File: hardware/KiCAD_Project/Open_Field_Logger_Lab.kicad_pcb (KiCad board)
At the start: 2 copper layers, 0 parts

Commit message: Initial PCB Layout
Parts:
- added BT1: 1-0000863, batteries:1-0000863, F.Cu at (133.6, 86.0)
- added C1: 1-0000007, capacitors_0603:1-0000007, F.Cu at (132.9, 113.2)
- added C16: 1-0000007, capacitors_0603:1-0000007, F.Cu at (171.7, 113.8)
- added C2: 1-0000007, capacitors_0603:1-0000007, F.Cu at (149.6, 105.3)
- added C3: 1-0001902, capacitors_0603:1-0001902, F.Cu at (137.2, 107.7)
- added C4: 1-0001902, capacitors_0603:1-0001902, F.Cu at (137.2, 110.5)
- added C5: 1-0000019, capacitors_0603:1-0000019, F.Cu at (102.6, 87.2)
- added D1: 1-0000600, leds_0805:1-0000600, F.Cu at (168.9, 69.1)
- added D2: 1-0000599, leds_0805:1-0000599, F.Cu at (179.1, 69.1)
- added D3: 1-0001188, leds_th:1-0001188, F.Cu at (191.8, 69.1)
- added D4: 1-0001896, diodes:1-0001896, F.Cu at (116.2, 97.7)
- added FID1: Fiducial_1mm_2mm, mechanical:Fiducial_1mm_Mask2mm, F.Cu at (101.0, 129.5)
- added FID2: Fiducial_1mm_2mm, mechanical:Fiducial_1mm_Mask2mm, F.Cu at (198.1, 70.6)
- added G***: LOGO, pcb_graphics:PCB Logo Standard, F.Cu at (104.6, 69.5)
- added H1: Imperial4, mechanical:MountingHole_imperial4, F.Cu at (96.5, 129.5)
- added H2: Imperial4, mechanical:MountingHole_imperial4, F.Cu at (198.1, 66.0)
- added H3: Imperial4, mechanical:MountingHole_imperial4, F.Cu at (96.5, 66.0)
- added H4: Imperial4, mechanical:MountingHole_imperial4, F.Cu at (198.1, 129.5)
- added J1: 1-0001899, connectors:1-0001899, F.Cu at (97.3, 97.8)
- added J10: 1-0001894, connectors:1-0001894, F.Cu at (109.3, 93.2)
- added J11: 1-0000127, connectors:1-0000127, F.Cu at (161.4, 116.0)
- added J12: NP_Conn_01x06, np_connectors:PinHeader_1x06_P2.54mm_Vertical, F.Cu at (177.5, 130.6)
- added J13: NP_Conn_01x03, np_connectors:PinHeader_1x03_P2.54mm_Vertical, F.Cu at (148.0, 64.9)
- added J14: AUX Input, np_connectors:PinHeader_1x04_P2.54mm_Vertical, F.Cu at (157.0, 105.8)
- added J2: 1-0001899, connectors:1-0001899, F.Cu at (109.5, 128.8)
- added J3: 1-0001899, connectors:1-0001899, F.Cu at (119.9, 128.8)
- added J4: 1-0001899, connectors:1-0001899, F.Cu at (130.3, 128.8)
- added J5: 1-0001899, connectors:1-0001899, F.Cu at (140.7, 128.8)
- added J6: 1-0001899, connectors:1-0001899, F.Cu at (151.1, 128.8)
- added J7: Conn_01x01, np_connectors:NP_Conn_ProtoPad, F.Cu at (96.5, 118.4)
- added J8: NP_Conn_01x04, np_connectors:PinHeader_1x04_P2.54mm_Vertical, F.Cu at (199.1, 122.2)
- added J9: 1-0001894, connectors:1-0001894, F.Cu at (109.3, 102.3)
- added MI1: 1-0001895, misc:misc_component, F.Cu at (109.3, 97.5)
- added PCB1: barepcb, misc:barepcb, F.Cu at (162.9, 169.9)
- added Q1: 1-0000163, mosfets:1-0000163, F.Cu at (127.5, 107.7)
- added Q2: 1-0000163, mosfets:1-0000163, F.Cu at (132.1, 107.7)
- added Q3: 1-0000163, mosfets:1-0000163, F.Cu at (122.9, 107.7)
- added R1: 1-0001184, resistors_0603:1-0001184, F.Cu at (107.2, 114.6)
- added R10: 1-0000010, resistors_0603:1-0000010, F.Cu at (127.5, 110.2)
- added R11: 1-0000010, resistors_0603:1-0000010, F.Cu at (122.9, 105.2)
- added R12: 1-0000010, resistors_0603:1-0000010, F.Cu at (122.9, 110.2)
- added R13: 1-0000174, resistors_0603:1-0000174, F.Cu at (171.7, 112.0)
- added R14: 1-0000010, resistors_0603:1-0000010, F.Cu at (159.0, 127.3)
- added R15: 1-0000010, resistors_0603:1-0000010, F.Cu at (152.6, 108.8)
- added R2: 1-0000008, resistors_0603:1-0000008, F.Cu at (165.6, 69.1)
- added R20: 1-0000174, resistors_0603:1-0000174, F.Cu at (161.8, 113.8)
- added R21: 1-0000010, resistors_0603:1-0000010, F.Cu at (132.1, 105.2)
- added R24: 1-0000010, resistors_0603:1-0000010, F.Cu at (132.1, 110.2)
- added R3: 1-0000008, resistors_0603:1-0000008, F.Cu at (175.8, 69.1)
- added R4: 1-0000369, resistors_0603:1-0000369, F.Cu at (185.7, 69.1)
- added R5: 1-0000010, resistors_0603:1-0000010, F.Cu at (131.3, 116.5)
- added R6: 1-0000010, resistors_0603:1-0000010, F.Cu at (129.8, 116.5)
- added R7: 1-0000010, resistors_0603:1-0000010, F.Cu at (125.2, 116.5)
- added R8: 1-0000010, resistors_0603:1-0000010, F.Cu at (123.7, 116.5)
- added R9: 1-0000010, resistors_0603:1-0000010, F.Cu at (127.5, 105.2)
- added SW1: 1-0000681, switches:1-0000681, F.Cu at (156.2, 69.1)
- added TH1: 1-0001897, sensors:1-0001897, F.Cu at (95.5, 114.6)
- added U1: 1-0001891, adcs:1-0001891, F.Cu at (127.5, 113.2)
- added U2: 1-0001892, rtcs:1-0001892, F.Cu at (142.7, 107.9)
- added U3: 1-0001893, dc_dc_converters:1-0001893, F.Cu at (106.9, 83.7)
- added U4: 1-0001890, microcontrollers:1-0001890, F.Cu at (175.6, 87.6)
- added Y1: 1-0001901, crystals_resonators:1-0001901, F.Cu at (140.0, 109.1)
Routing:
- net I2C_SDA: track 0.00 -> 129.8 mm, vias 0 -> 3
- net I2C_SCL: track 0.00 -> 125.0 mm, vias 0 -> 3
- net SPI_MOSI: track 0.00 -> 86.8 mm, vias 0 -> 6
- net SPI_MISO: track 0.00 -> 78.5 mm, vias 0 -> 1
- net SPI_SCK: track 0.00 -> 75.3 mm, vias 0 -> 3
- net ADC_ALRT: track 0.00 -> 59.7 mm
- net Error_LED: track 0.00 -> 48.6 mm
- net SD_CS: track 0.00 -> 43.9 mm, vias 0 -> 1
- net Log_LED: track 0.00 -> 40.8 mm
- net EXT_CS: track 0.00 -> 37.0 mm, vias 0 -> 1
- net SD_CD: track 0.00 -> 35.6 mm, vias 0 -> 3
- net RTC_MFP: track 0.00 -> 32.1 mm, vias 0 -> 2
- net Log_Button: track 0.00 -> 30.9 mm
- net Net-(BT1-+): track 0.00 -> 29.4 mm, vias 0 -> 2
- net RX: track 0.00 -> 27.5 mm
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- added copper zone on In1.Cu, net +3V3
- added copper zone on In2.Cu, net +5V
- added copper zone on B.Cu, net GND
- added copper zone on F.Cu, net GND
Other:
- board outline added: 107.9 x 69.8 mm
- copper layers 2 -> 4
- board text added: "(Low Current Only)"
- board text added: "0-5V Analog Inputs"
- board text added: "32.768kHz Crystal"
- board text added: "3V3"
- board text added: "5V Sensor Out"
- board text added: "AIN0"
- board text added: "AIN1"
- board text added: "AIN2"
- board text added: "AIN3"
- board text added: "ATC/ATO 1A Fuse"
- board text added: "CS"
- board text added: "DC DC Converter (5V)"
- board text added: "Error"
- board text added: "GND"
- board text added: "Hole Spacing: 4{dblquote} x 2.5{dblquote} Board Dimensions: 4.25{dblquote} x 2.75{dblquote}"
- board text added: "I2C"
- board text added: "IO34"
- board text added: "IO35"
- board text added: "IO36"
- board text added: "IO39"
- board text added: "Input 9V - 18V"
- board text added: "Leeman Geophysical LLC Open Field Logger Lab Rev 1.0"
- board text added: "Logging"
- board text added: "MISO"
- board text added: "MOSI"
- board text added: "NTC: 10K B = 3950k"
- board text added: "Power"
- board text added: "RP Diode"
- board text added: "RTC"
- board text added: "RTC Battery CR2032"
- board text added: "RX"
- board text added: "SCK"
- board text added: "SCL"
- board text added: "SDA"
- board text added: "SPI"
- board text added: "Spare GPIO"
- board text added: "Start/Stop"
- board text added: "TX"
- board text added: "Temp Out"
- board text added: "VDC"

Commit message: Updated PCB title block, Added PCB# silk
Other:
- board text added: "3-0000304"
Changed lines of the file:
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@@
 	(paper "USLetter")
 	(title_block
-		(date "2024-06-05")
+		(title "Open Field Logger Lab")
+		(date "2026-06-15")
 		(rev "1.0")
 		(company "Leeman Geophysical LLC")
@@
 		)
 	)
+	(gr_text "3-0000304"
+		(at 104.14 64.008 -0)
+		(layer "B.SilkS")
+		(effects
+			(font
+				(size 1.016 1.016)
+				(thickness 0.254)
+				(bold yes)
+			)
+			(justify mirror)
+		)
+	)

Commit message: Rev 1.0 production files
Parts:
- renumbered C5 to C1, C16 to C5, C1 to C6, D3 to D1, D4 to D3, D1 to D4, H4 to H1, H3 to H2, H2 to H3, H1 to H4, J6 to J10, J2 to J11, J3 to J12, J4 to J13, J5 to J14, J9 to J2, J10 to J3, J14 to J4, J13 to J5, J12 to J6, J8 to J7, J11 to J8, J7 to J9, Q2 to Q1, Q1 to Q2, R4 to R1, R12 to R10, R14 to R11, R20 to R12, R1 to R14, R8 to R15, R7 to R16, R6 to R17, R5 to R18, R3 to R2, R15 to R3, R2 to R4, R21 to R5, R9 to R6, R11 to R7, R24 to R8, R10 to R9, U3 to U1, U4 to U2, U2 to U3, U1 to U4

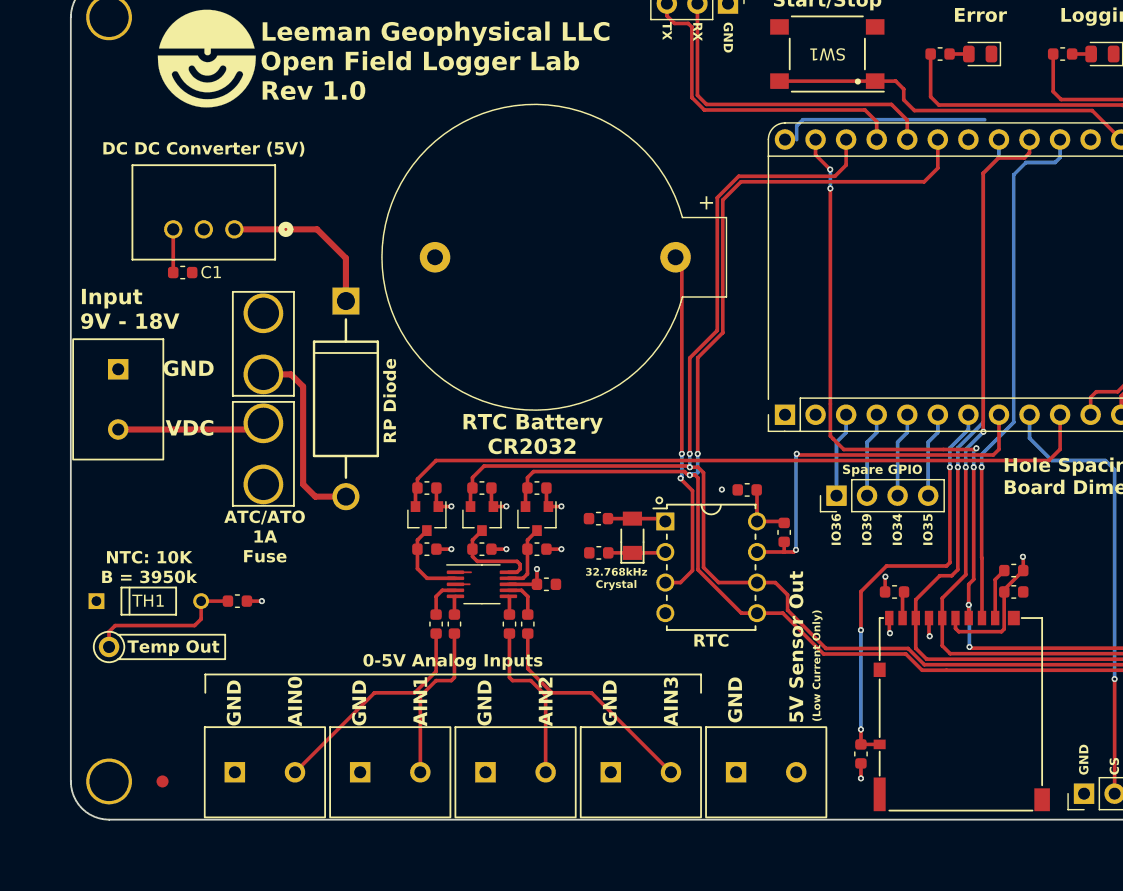
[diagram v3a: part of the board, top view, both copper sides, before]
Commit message: Fixed Issues: #2 #3 #4
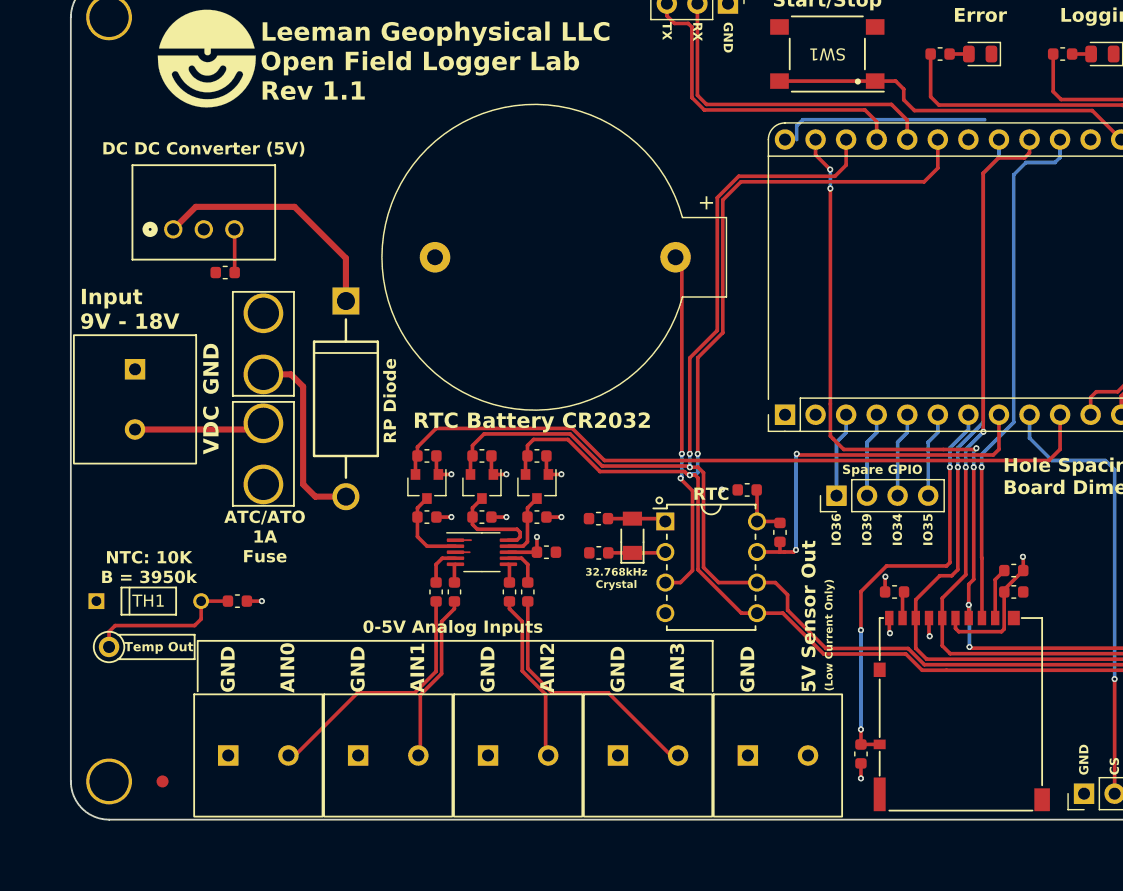
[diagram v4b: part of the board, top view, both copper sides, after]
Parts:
- moved C1 3.53 mm to (106.2, 87.2), turned to 180 degrees
- moved C6 2.67 mm to (132.9, 110.5)
- moved Q1 2.67 mm to (132.1, 105.0)
- moved Q2 2.67 mm to (127.5, 105.0)
- moved Q3 2.67 mm to (122.9, 105.0)
- moved R10 2.67 mm to (122.9, 107.6)
- moved R15 2.67 mm to (123.7, 113.8)
- moved R16 2.67 mm to (125.2, 113.8)
- moved R17 2.67 mm to (129.8, 113.8)
- moved R18 2.67 mm to (131.3, 113.8)
- moved R5 2.67 mm to (132.1, 102.5)
- moved R6 2.67 mm to (127.5, 102.5)
- moved R7 2.67 mm to (122.9, 102.5)
- moved R8 2.67 mm to (132.1, 107.6)
- moved R9 2.67 mm to (127.5, 107.6)
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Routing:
- net Net-(U1-Vin): track 13.8 -> 20.5 mm
- net Net-(J11-Pin_2): track 18.3 -> 20.4 mm
- net Net-(J14-Pin_2): track 18.4 -> 20.5 mm
- net Net-(J1-Pin_2): track 12.3 -> 10.9 mm
- net I2C_SDA: track 129.8 -> 130.9 mm
- net I2C_SCL: track 125.0 -> 126.1 mm
- net ADC_ALRT: track 59.7 -> 60.8 mm
- net Net-(J12-Pin_2): track 13.4 -> 14.0 mm
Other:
- board text added: "3-0000307"
- board text added: "Leeman Geophysical LLC Open Field Logger Lab Rev 1.1"
- board text removed: "3-0000304"
- board text removed: "Leeman Geophysical LLC Open Field Logger Lab Rev 1.0"
